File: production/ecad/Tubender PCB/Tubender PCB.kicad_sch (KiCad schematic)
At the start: 0 parts

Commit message: sensor updates!
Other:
- sheet SENSORS ports: added 3.3V; removed none
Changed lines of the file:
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@@
 	(wire
 		(pts
-			(xy 90.17 92.71) (xy 90.17 95.25)
+			(xy 87.63 92.71) (xy 87.63 95.25)
 		)
 		(stroke
@@
 	(wire
 		(pts
-			(xy 87.63 93.98) (xy 87.63 95.25)
+			(xy 85.09 93.98) (xy 85.09 95.25)
 		)
 		(stroke
@@
 	(wire
 		(pts
+			(xy 90.17 93.98) (xy 90.17 95.25)
+		)
+		(stroke
+			(width 0)
+			(type default)
+		)
+	)
+	(wire
+		(pts
 			(xy 105.41 83.82) (xy 106.68 83.82)
 		)
@@
 	(wire
 		(pts
-			(xy 85.09 93.98) (xy 85.09 95.25)
+			(xy 82.55 93.98) (xy 82.55 95.25)
 		)
 		(stroke
@@
 	(global_label "3.3V"
 		(shape input)
+		(at 90.17 93.98 90)
+		(fields_autoplaced yes)
+		(effects
+			(font
+				(size 1.27 1.27)
+			)
+			(justify left)
+		)
+		(property "Intersheetrefs" "${INTERSHEET_REFS}"
+			(at 90.17 86.8824 90)
+			(effects
+				(font
+					(size 1.27 1.27)
+				)
+				(justify left)
+				(hide yes)
+			)
+		)
+	)
+	(global_label "3.3V"
+		(shape input)
 		(at 93.98 33.02 0)
 		(fields_autoplaced yes)
@@
 	(global_label "12V"
 		(shape input)
-		(at 87.63 93.98 90)
+		(at 85.09 93.98 90)
 		(fields_autoplaced yes)
 		(effects
@@
 		)
 		(property "Intersheetrefs" "${INTERSHEET_REFS}"
-			(at 87.63 87.4872 90)
+			(at 85.09 87.4872 90)
 			(effects
 				(font
@@
 	(global_label "24V"
 		(shape input)
-		(at 85.09 93.98 90)
+		(at 82.55 93.98 90)
 		(fields_autoplaced yes)
 		(effects
@@
 		)
 		(property "Intersheetrefs" "${INTERSHEET_REFS}"
-			(at 85.09 87.4872 90)
+			(at 82.55 87.4872 90)
 			(effects
 				(font
@@
 	(global_label "5V"
 		(shape input)
-		(at 90.17 92.71 90)
+		(at 87.63 92.71 90)
 		(fields_autoplaced yes)
 		(effects
@@
 		)
 		(property "Intersheetrefs" "${INTERSHEET_REFS}"
-			(at 90.17 87.4267 90)
+			(at 87.63 87.4267 90)
 			(effects
 				(font
@@
 		)
 		(pin "12V" input
+			(at 85.09 95.25 90)
+			(effects
+				(font
+					(size 1.27 1.27)
+				)
+				(justify right)
+			)
+		)
+		(pin "24V" input
+			(at 82.55 95.25 90)
+			(effects
+				(font
+					(size 1.27 1.27)
+				)
+				(justify right)
+			)
+		)
+		(pin "5V" input
 			(at 87.63 95.25 90)
-			(effects
-				(font
-					(size 1.27 1.27)
-				)
-				(justify right)
-			)
-		)
-		(pin "24V" input
-			(at 85.09 95.25 90)
-			(effects
-				(font
-					(size 1.27 1.27)
-				)
-				(justify right)
-			)
-		)
-		(pin "5V" input
-			(at 90.17 95.25 90)
 			(effects
 				(font
@@
 			(effects
 				(font
+					(size 1.27 1.27)
+				)
+				(justify right)
+			)
+		)
+		(pin "3.3V" input
+			(at 90.17 95.25 90)
+			(effects
+				(font

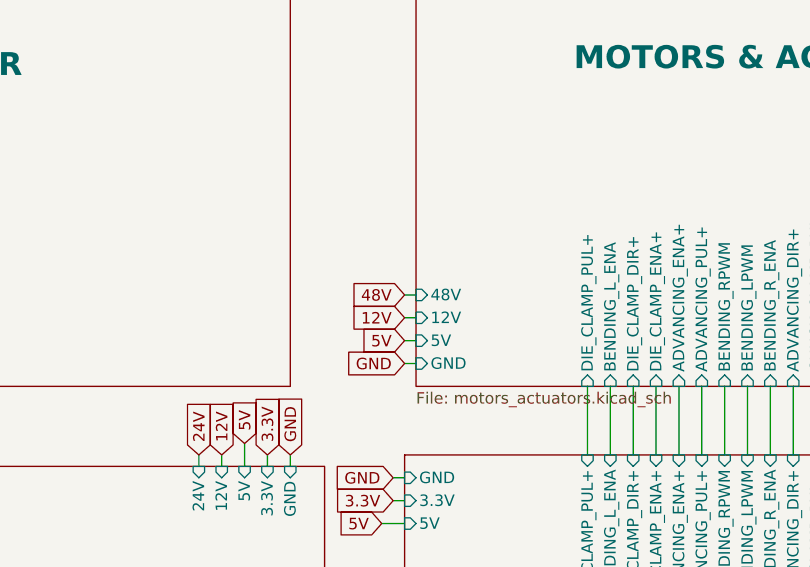
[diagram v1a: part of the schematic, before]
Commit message: 0 Ohm Resistors
Added DNP 0 Ohm's connected to the 24V rail to the motor connectors power out pin. This is in case we have issues with the drivers taking 48 volts and to just have flexbility
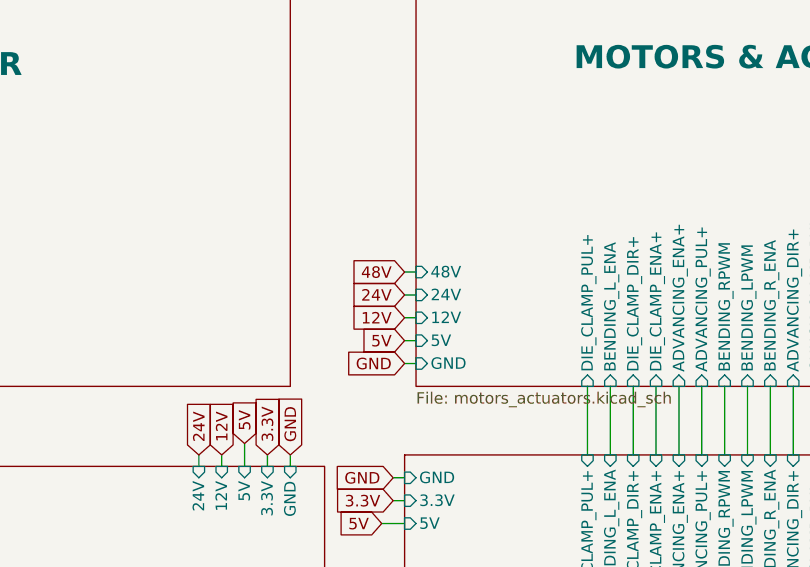
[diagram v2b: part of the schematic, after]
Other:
- sheet MOTORS & ACTUATORS ports: added 24V; removed none
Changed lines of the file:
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@@
+	(wire
+		(pts
+			(xy 105.41 76.2) (xy 106.68 76.2)
+		)
+		(stroke
+			(width 0)
+			(type default)
+		)
+	)
 	(wire
 		(pts
@@
 	(wire
 		(pts
-			(xy 105.41 76.2) (xy 106.68 76.2)
+			(xy 105.41 73.66) (xy 106.68 73.66)
 		)
 		(stroke
@@
 		)
 	)
+	(global_label "24V"
+		(shape input)
+		(at 105.41 76.2 180)
+		(fields_autoplaced yes)
+		(effects
+			(font
+				(size 1.27 1.27)
+			)
+			(justify right)
+		)
+		(property "Intersheetrefs" "${INTERSHEET_REFS}"
+			(at 98.9172 76.2 0)
+			(effects
+				(font
+					(size 1.27 1.27)
+				)
+				(justify right)
+				(hide yes)
+			)
+		)
+	)
 	(global_label "GND"
 		(shape input)
@@
 	(global_label "48V"
 		(shape input)
-		(at 105.41 76.2 180)
+		(at 105.41 73.66 180)
 		(fields_autoplaced yes)
 		(effects
@@
 		)
 		(property "Intersheetrefs" "${INTERSHEET_REFS}"
-			(at 98.9172 76.2 0)
+			(at 98.9172 73.66 0)
 			(effects
 				(font
@@
 		)
 		(pin "48V" input
-			(at 106.68 76.2 180)
+			(at 106.68 73.66 180)
 			(effects
 				(font
@@
 			(effects
 				(font
+					(size 1.27 1.27)
+				)
+				(justify left)
+			)
+		)
+		(pin "24V" input
+			(at 106.68 76.2 180)
+			(effects
+				(font
